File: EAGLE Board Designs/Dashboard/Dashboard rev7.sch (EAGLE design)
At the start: 115 parts, among them J1 CONNECTOR-4_μF_S_RA_, J10 CONNECTOR-10__, J2 CONNECTOR-8_μF_S_RA_, J3 CONNECTOR-4_μF_S_RA_, J4 CONNECTOR-6_μF_S_RA_, J5 CONNECTOR-10__, J6 CONNECTOR-6_μF_S_RA_, J7 CONNECTOR-4_538-505110-0492_, J8 USB4110, J9 CONNECTOR-4_538-505110-0492_, U1 NEOPIXEL_IN-PI55QATPRPGPBPW-40, U10 NEOPIXEL_IN-PI55QATPRPGPBPW-40, U12 NEOPIXEL_IN-PI55QATPRPGPBPW-40, U13 NEOPIXEL_IN-PI55QATPRPGPBPW-40, U14 NEOPIXEL_IN-PI55QATPRPGPBPW-40, U15 NEOPIXEL_IN-PI55QATPRPGPBPW-40, U16 STM32-LQFP64, U17 VOLTAGE_REGULATOR_SOT-223_3.3V, U2 NEOPIXEL_IN-PI55QATPRPGPBPW-40, U27 TCAN1051HQV-Q1, U3 MCP23S08, U4 NEOPIXEL_IN-PI55QATPRPGPBPW-40, U5 RE46C100, U6 NEOPIXEL_IN-PI55QATPRPGPBPW-40, U7 NEOPIXEL_IN-PI55QATPRPGPBPW-40, U8 NEOPIXEL_IN-PI55QATPRPGPBPW-40, U9 NEOPIXEL_IN-PI55QATPRPGPBPW-40, X1 24_MHZ_XTAL_OSCILLATOR

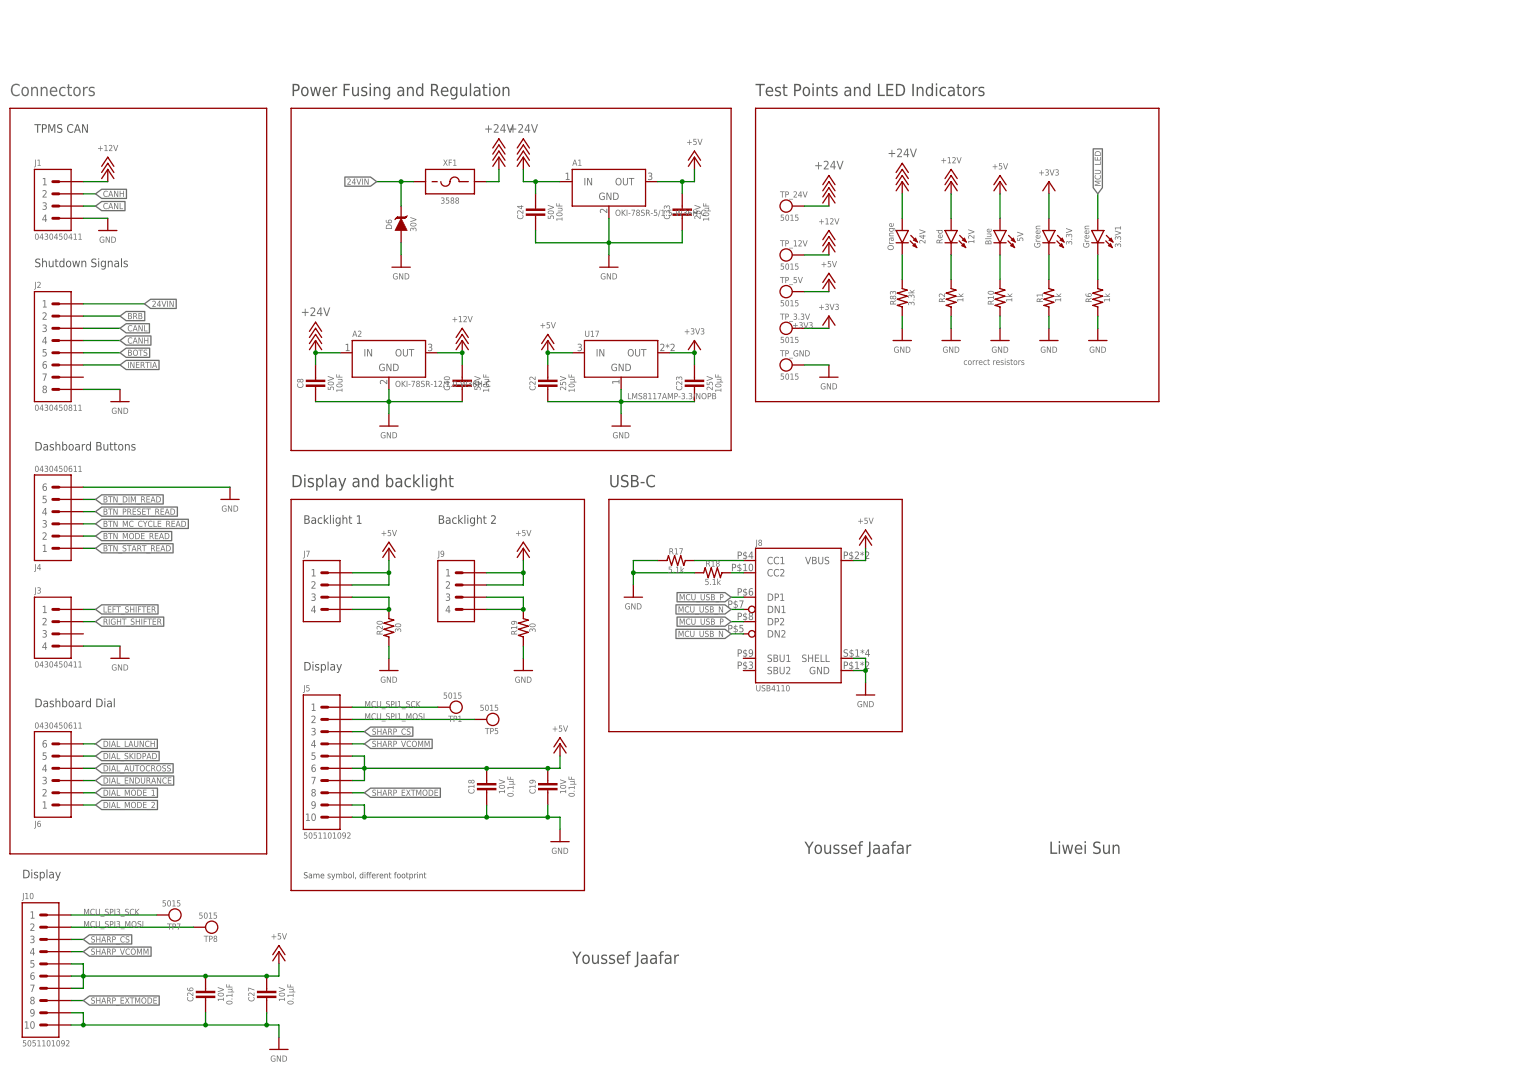
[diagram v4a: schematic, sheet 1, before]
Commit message: Finishing touches, silkscreen modification, changed dial connector, added decoupling cap
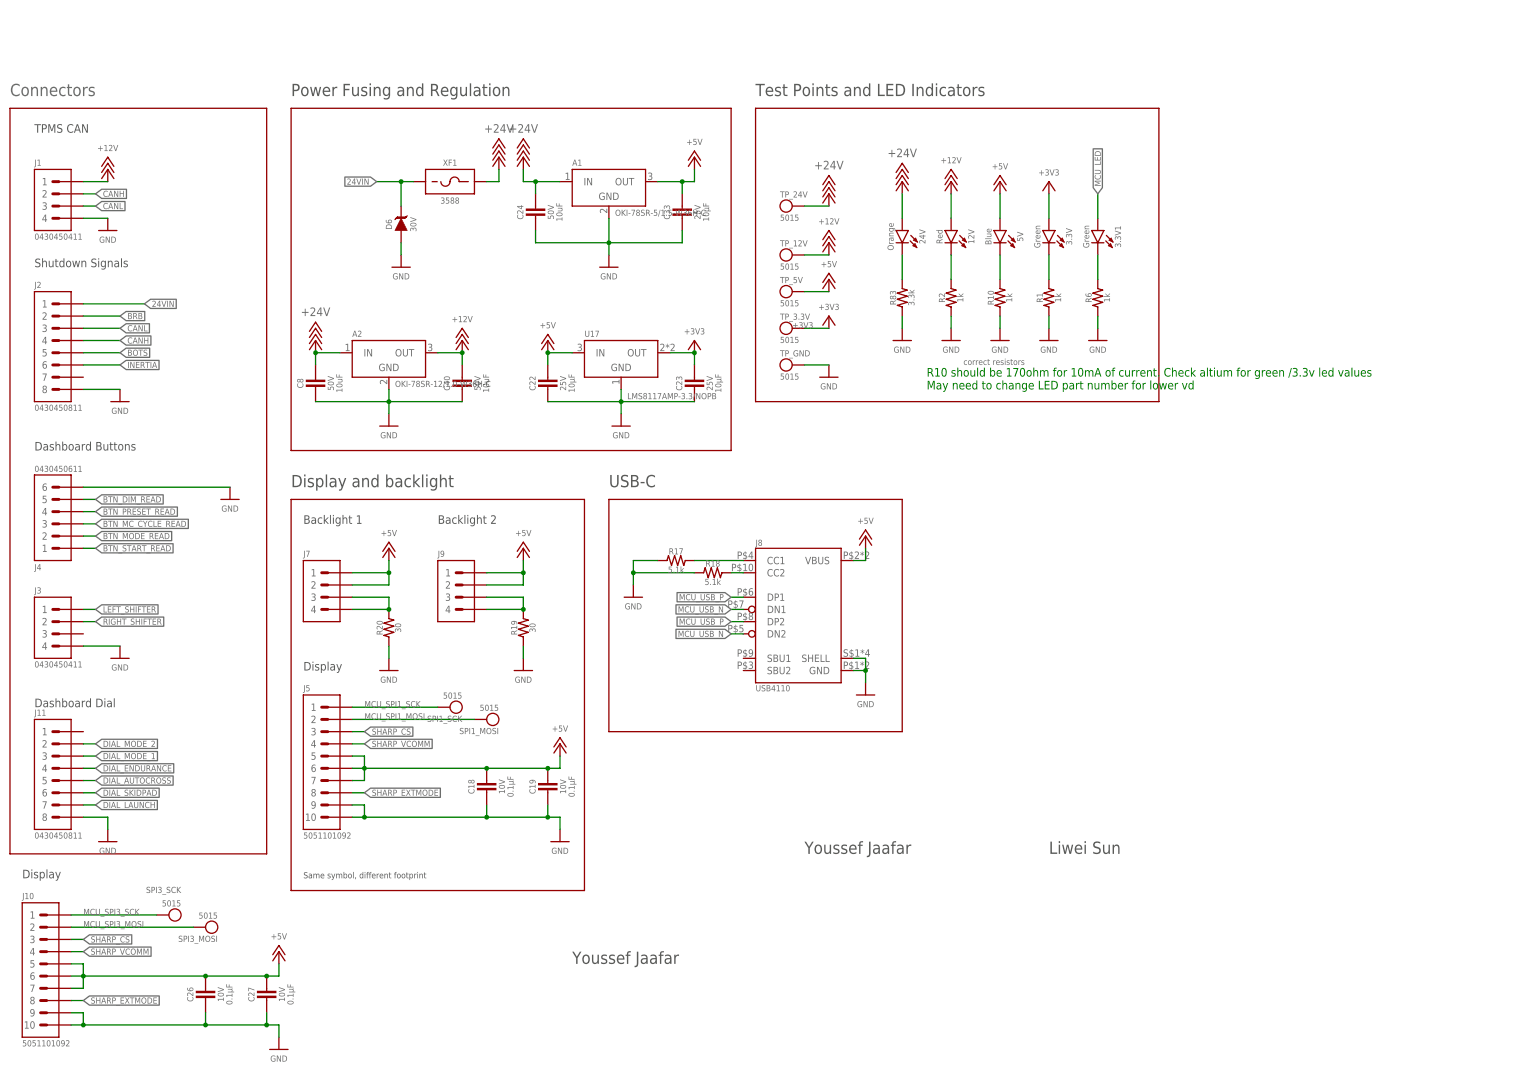
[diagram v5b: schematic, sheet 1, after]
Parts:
- removed J6: CONNECTOR-6_μF_S_RA_, HyTechDevices:CONNECTOR-6_μF_S_RA_
- added C28: CAPACITOR_0603_10V_0.1UF, HyTechDevices:CAPACITOR_0603_10V_0.1UF
- added J11: CONNECTOR-8_μF_S_RA_, HyTechDevices:CONNECTOR-8_μF_S_RA_
- renumbered TP1 to SPI1_SCK, TP2 to INERTIA, TP3 to BOTS, TP4 to BRB, TP5 to SPI1_MOSI, TP6 to NEOPIXELS, TP7 to SPI3_SCK, TP8 to SPI3_MOSI
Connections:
- removed net VBAT: U16.VBAT
- net +3V3: now also C28.1, U16.VBAT
- net DIAL_AUTOCROSS: now also J11.5; no longer J6.4
- net DIAL_ENDURANCE: now also J11.4; no longer J6.3
- net DIAL_LAUNCH: now also J11.7; no longer J6.6
- net DIAL_MODE_1: now also J11.3; no longer J6.2
- net DIAL_MODE_2: now also J11.2; no longer J6.1
- net DIAL_SKIDPAD: now also J11.6; no longer J6.5
- net GND: now also C28.2, J11.8
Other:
- note added: "R10 should be 170ohm for 10mA of current. Check altium for green /3.3v led values May need to change LED part number for lower vd"
- moved on the sheet: C13

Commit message: small changes
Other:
- note added: "Walker Burns"
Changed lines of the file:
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@@
 <text x="17.78" y="129.54" size="1.778" layer="97">Dashboard Buttons</text>
 <text x="17.78" y="76.2" size="1.778" layer="97">Dashboard Dial</text>
-<text x="129.54" y="22.86" size="2.54" layer="97">Youssef Jaafar</text>
-<text x="228.6" y="45.72" size="2.54" layer="97">Liwei Sun</text>
-<text x="177.8" y="45.72" size="2.54" layer="97">Youssef Jaafar</text>
+<text x="177.8" y="45.72" size="2.54" layer="97">Ivan Mix</text>
 <text x="210.82" y="147.32" size="1.27" layer="95">correct resistors</text>
 <wire x1="162.56" y1="129.54" x2="162.56" y2="200.66" width="0.1524" layer="94"/>
@@
 <text x="203.2" y="142.24" size="1.778" layer="91">R10 should be 170ohm for 10mA of current. Check altium for green /3.3v led values
 May need to change LED part number for lower vd</text>
+<text x="177.8" y="38.1" size="2.54" layer="97">Walker Burns</text>
 </plain>
 <instances>
@@
 <sheet>
 <plain>
-<text x="180.34" y="45.72" size="2.54" layer="95" font="vector">Ivan Mix</text>
 <text x="17.78" y="162.56" size="1.27" layer="95" rot="R270">Change to 10 pF</text>
 <wire x1="172.72" y1="119.38" x2="254" y2="119.38" width="0.1524" layer="94"/>
@@
 <wire x1="167.64" y1="73.66" x2="7.62" y2="73.66" width="0.1524" layer="94"/>
 <text x="7.62" y="205.74" size="2.54" layer="97">MCU</text>
+<text x="177.8" y="45.72" size="2.54" layer="97">Ivan Mix</text>
+<text x="177.8" y="38.1" size="2.54" layer="97">Walker Burns</text>
 </plain>
 <instances>
@@
 <text x="12.7" y="88.9" size="1.778" layer="97">24V to 3.3V</text>
 <text x="15.24" y="63.5" size="1.778" layer="97">24V to 3.3V</text>
-<text x="228.6" y="45.72" size="2.54" layer="97">Liwei Sun</text>
-<text x="177.8" y="45.72" size="2.54" layer="97">Youssef Jaafar</text>
-<text x="132.08" y="22.86" size="2.54" layer="97">Youssef Jaafar</text>
 <text x="167.64" y="104.14" size="1.778" layer="97">Error Codes</text>
 <wire x1="10.16" y1="200.66" x2="71.12" y2="200.66" width="0.1524" layer="94"/>
@@
 <wire x1="170.18" y1="60.96" x2="205.74" y2="60.96" width="0.1524" layer="94"/>
 <text x="91.44" y="119.38" size="2.54" layer="97">7-SEG</text>
+<text x="177.8" y="45.72" size="2.54" layer="97">Ivan Mix</text>
+<text x="177.8" y="38.1" size="2.54" layer="97">Walker Burns</text>
 </plain>
 <instances>
@@
 <text x="88.9" y="177.8" size="1.778" layer="97">BRAKE_ENGAGE</text>
 <text x="210.82" y="177.8" size="1.778" layer="97">LAUNCH_CTRL</text>
-<text x="236.22" y="45.72" size="2.54" layer="97">Liwei Sun</text>
-<text x="185.42" y="45.72" size="2.54" layer="97">Youssef Jaafar</text>
-<text x="132.08" y="22.86" size="2.54" layer="97">Youssef Jaafar</text>
+<text x="177.8" y="45.72" size="2.54" layer="97">Ivan Mix</text>
+<text x="177.8" y="38.1" size="2.54" layer="97">Walker Burns</text>
 </plain>
 <instances>

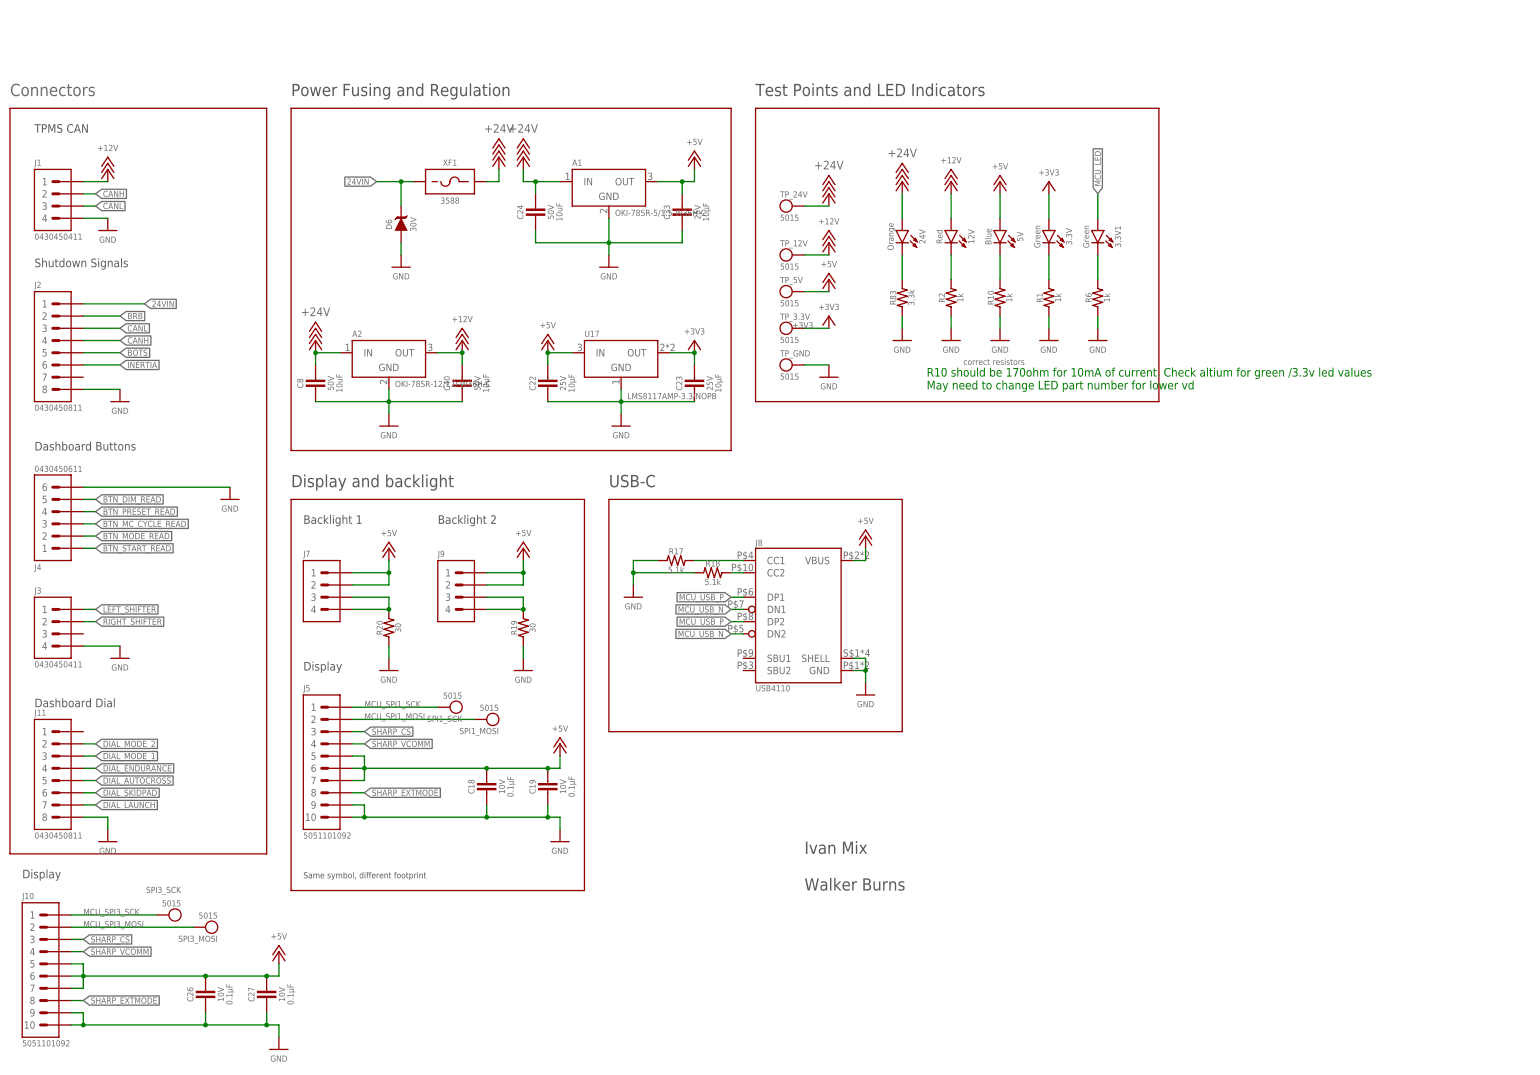
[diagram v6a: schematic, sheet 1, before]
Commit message: Added jumper and shottky for bypassing VBUS capacitance
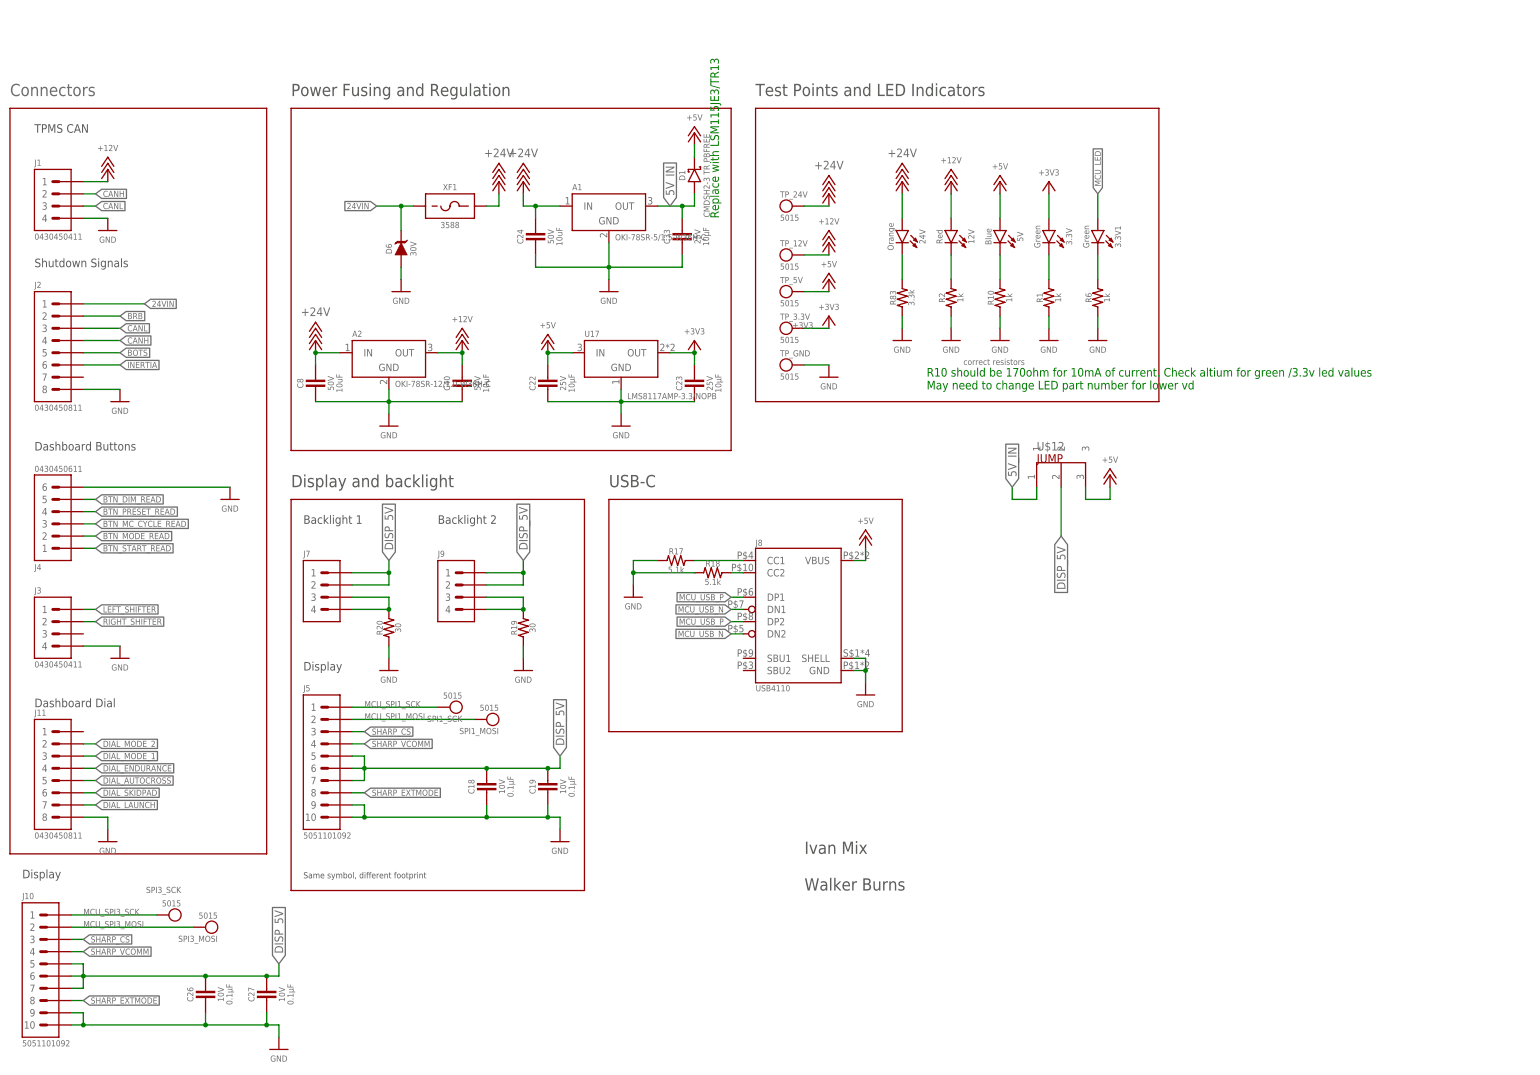
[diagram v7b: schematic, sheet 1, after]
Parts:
- added D1: SCHOTTKY_SOD323_30VV, HyTechDevices:SCHOTTKY_SOD323_30VV
- added U$12: JUMPER_3PIN, HyTechDevices:JUMPER_3PIN
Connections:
- new net 5V_IN: A1.OUT, C33.1, D1.A, U$12.1
- new net DISP_5V: C18.1, C19.1, C26.1, C27.1, J10.5, J10.6, J10.7, J5.5, J5.6, J5.7, J7.1, J7.2, J9.1, J9.2, U$12.2
- net +5V: now also D1.C, U$12.3; no longer A1.OUT, C18.1, C19.1, C26.1, C27.1, C33.1, J10.5, J10.6, J10.7, J5.5, J5.6, J5.7, J7.1, J7.2, J9.1, J9.2
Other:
- note added: "Replace with LSM115JE3/TR13"
- moved on the sheet: A1, C24, C33, D6, XF1
